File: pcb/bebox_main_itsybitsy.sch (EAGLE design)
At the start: 30 parts, among them J1 SJ-435107RS, J2 SJ-435107RS, J4 SJ-435107RS, J6 PJ-102AH, P2 OSTTE020104, P3 OSTTE020104, P4 OSTTE020104, P5 OSTTE020104, Q1 2N7000, Q2 2N7000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

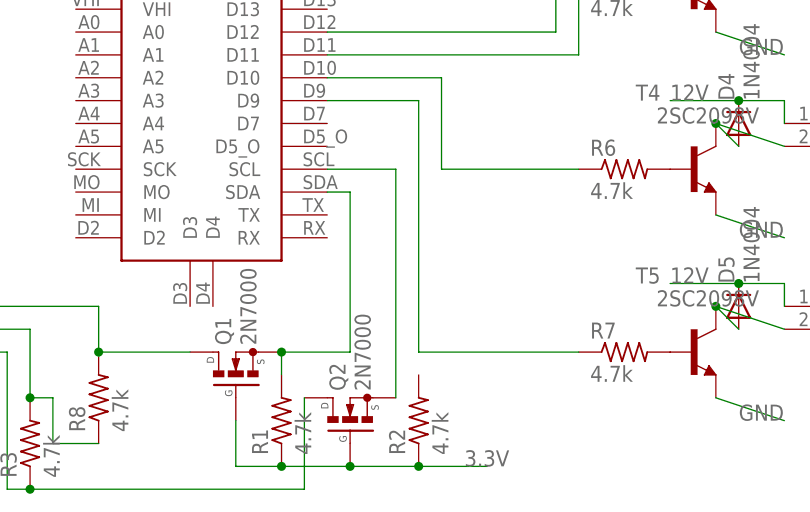
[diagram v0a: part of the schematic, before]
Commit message: Updated screenprints.
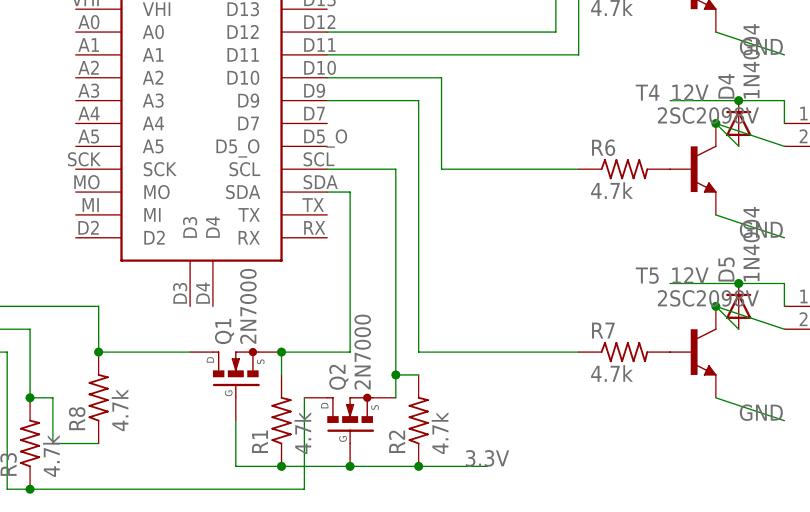
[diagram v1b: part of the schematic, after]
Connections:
- net N$3: now also R2.2
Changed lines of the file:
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@@
 <wire x1="91.44" y1="22.86" x2="99.06" y2="22.86" width="0.1524" layer="91"/>
 <pinref part="Q2" gate="G$1" pin="S"/>
-<wire x1="99.06" y1="22.86" x2="99.06" y2="-2.54" width="0.1524" layer="91"/>
+<wire x1="99.06" y1="22.86" x2="99.06" y2="0" width="0.1524" layer="91"/>
+<pinref part="R2" gate="G$1" pin="2"/>
+<wire x1="99.06" y1="0" x2="99.06" y2="-2.54" width="0.1524" layer="91"/>
+<wire x1="101.6" y1="0" x2="99.06" y2="0" width="0.1524" layer="91"/>
+<junction x="99.06" y="0"/>
 </segment>
 </net>
